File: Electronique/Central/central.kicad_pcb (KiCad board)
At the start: 2 copper layers, 173 x 90 mm, 66 parts, among them P1 CONN_02X03, P10 CONN_Selec, P11 CONN_01X02, P12 CONN_01X02, P13 CONN_01X02, P14 CONN_01X02, P15 CONN_01X02, P2 CONN_Speaker, P3 CONN_jack, P4 CONN_jacky_led, P5 CONN_LED, P6 CONN_02X03, P7 CONN_02X03, P8 CONN_02X03, P9 CONN_jack_start, Q1 IRF540N, Q2 Q_NMOS_DGS, Q3 Q_NMOS_DGS, U1 Nucleo-64, U10 trou-d3mm, U11 trou-d3mm, U12 trou-d3mm, U13 trou-d3mm, U14 trou-d3mm, U15 trou-d3mm, U2 LM317_SOT223, U3 LM317_SOT223, U4 TDA6205, U5 B_Plug_5mm, U6 B_Plug_5mm, U7 DSN2596, U8 DSN2596, U9 MC34152

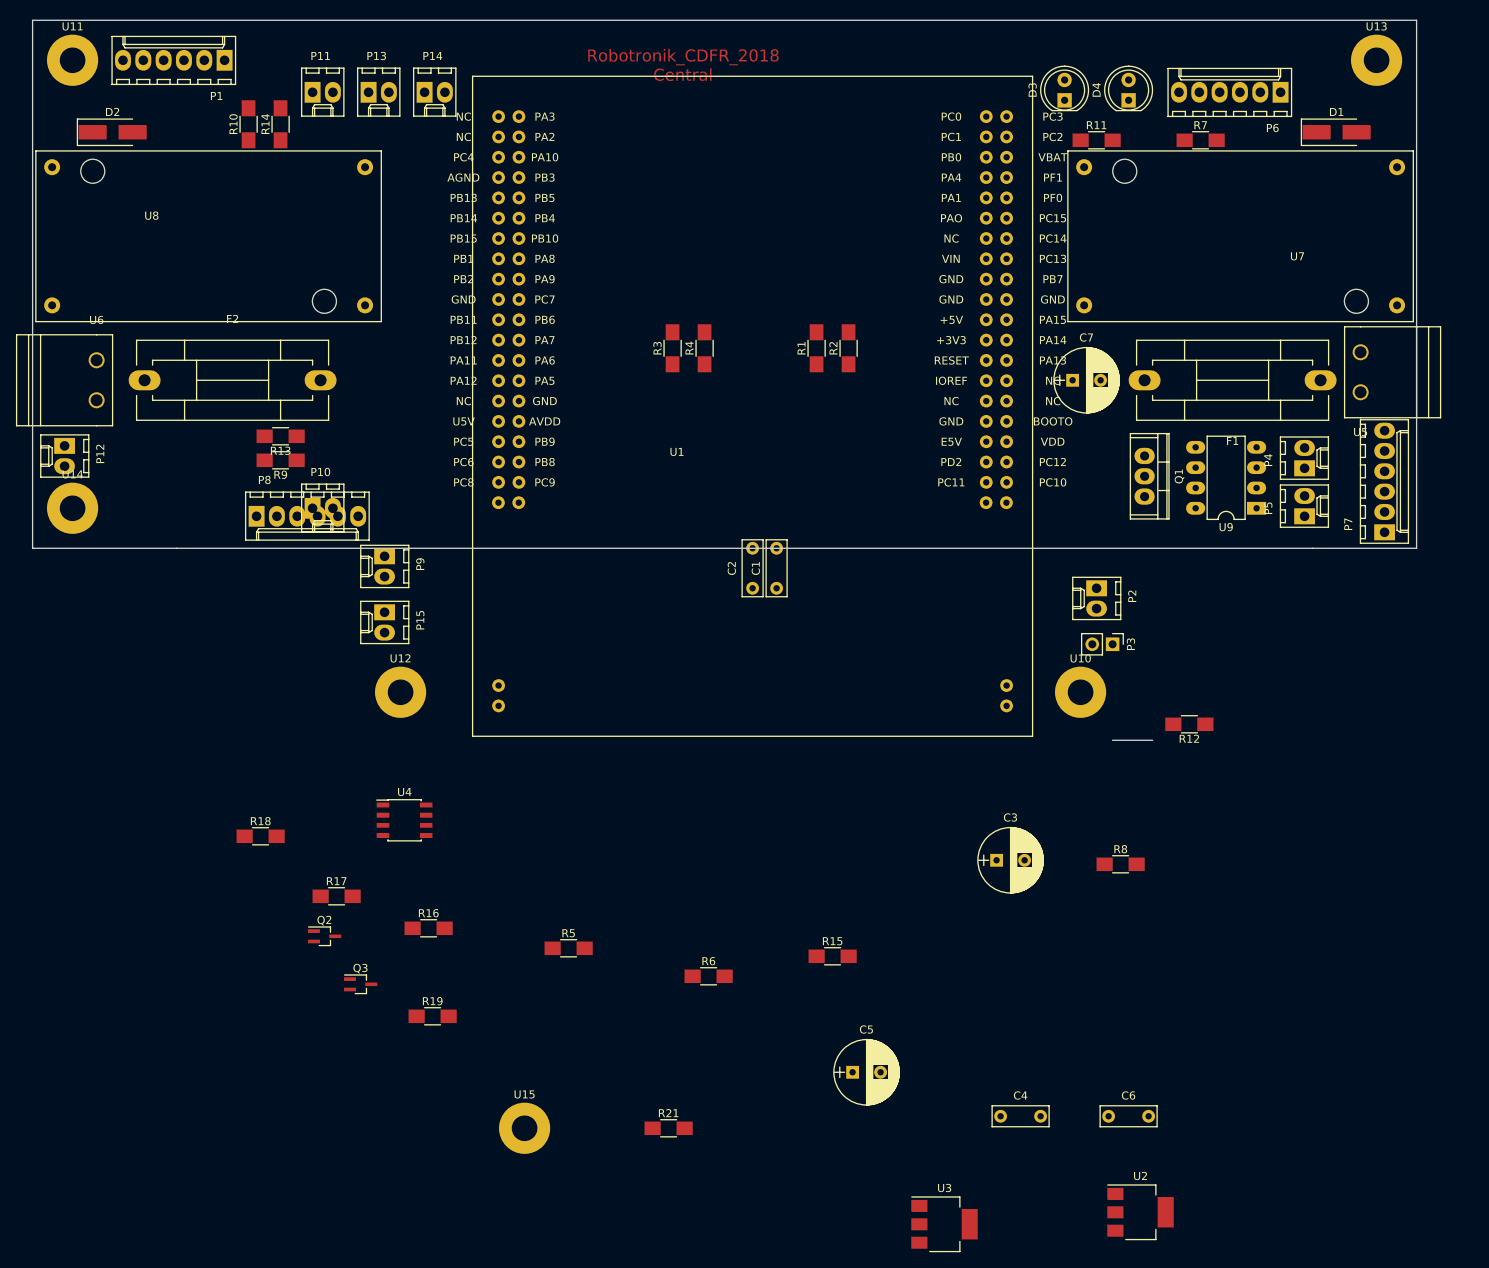
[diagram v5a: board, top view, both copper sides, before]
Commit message: Central : placement
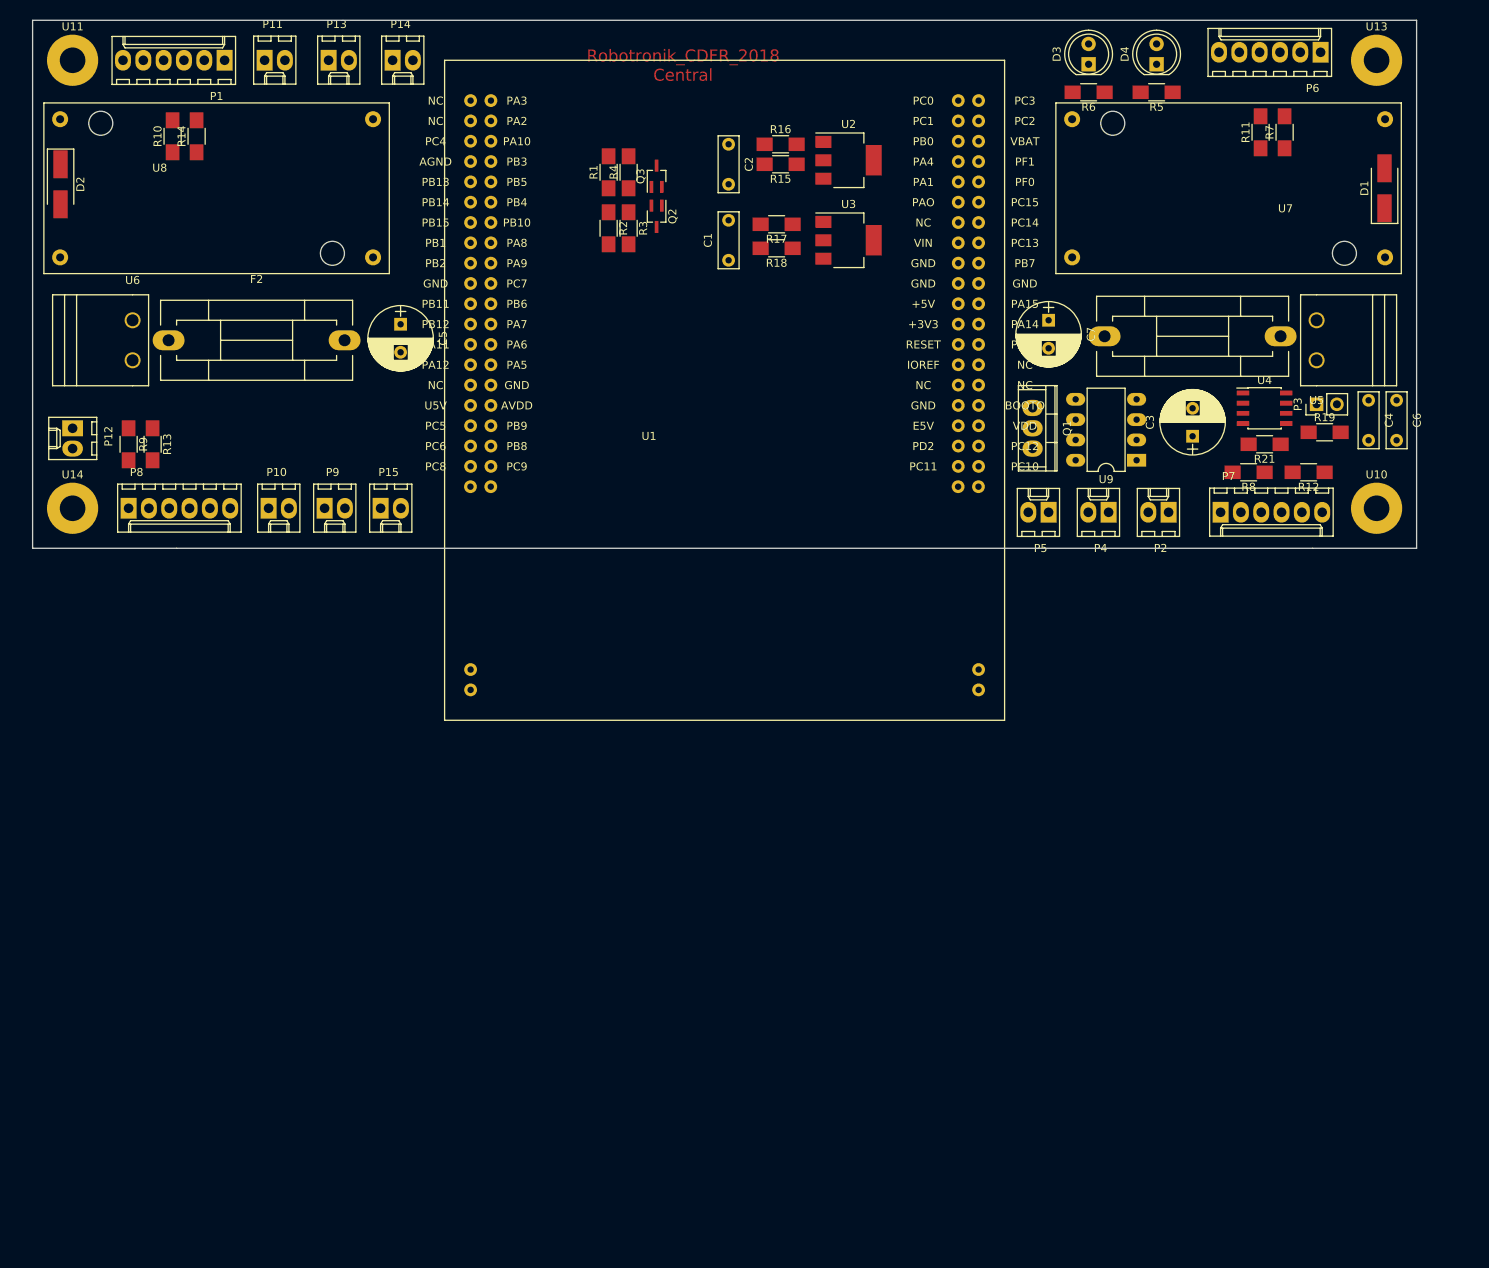
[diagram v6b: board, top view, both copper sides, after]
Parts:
- removed U12, U15: trou-d3mm, Mounting_Holes:MountingHole_3.2mm_M3_Pad
- moved U2 136.5 mm to (168.0, 85.5)
- moved R19 133.3 mm to (227.5, 119.5)
- moved R5 129.8 mm to (206.5, 77.0), turned to 180 degrees
- moved U3 123.6 mm to (168.0, 95.5)
- moved R6 120.3 mm to (198.0, 77.0), turned to 180 degrees
- moved U4 119.2 mm to (220.0, 116.5)
- moved R21 113.4 mm to (220.0, 121.0), turned to 180 degrees
- moved C5 109.2 mm to (112.0, 106.0), turned to 270 degrees
- moved Q3 107.6 mm to (144.0, 87.5), turned to 90 degrees
- moved R16 107.4 mm to (159.5, 83.5)
- moved C4 100.6 mm to (233.0, 115.5), turned to 270 degrees
- moved R17 100.4 mm to (159.0, 93.5), turned to 180 degrees
- moved R15 99.2 mm to (159.5, 86.0), turned to 180 degrees
- moved Q2 99.1 mm to (144.0, 92.5), turned to 270 degrees
- moved R18 97.8 mm to (159.0, 96.5), turned to 180 degrees
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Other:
- board size 173 x 90 mm -> 173 x 66 mm
- rule via_min_size: 0.4 -> 0.6

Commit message: Central routage
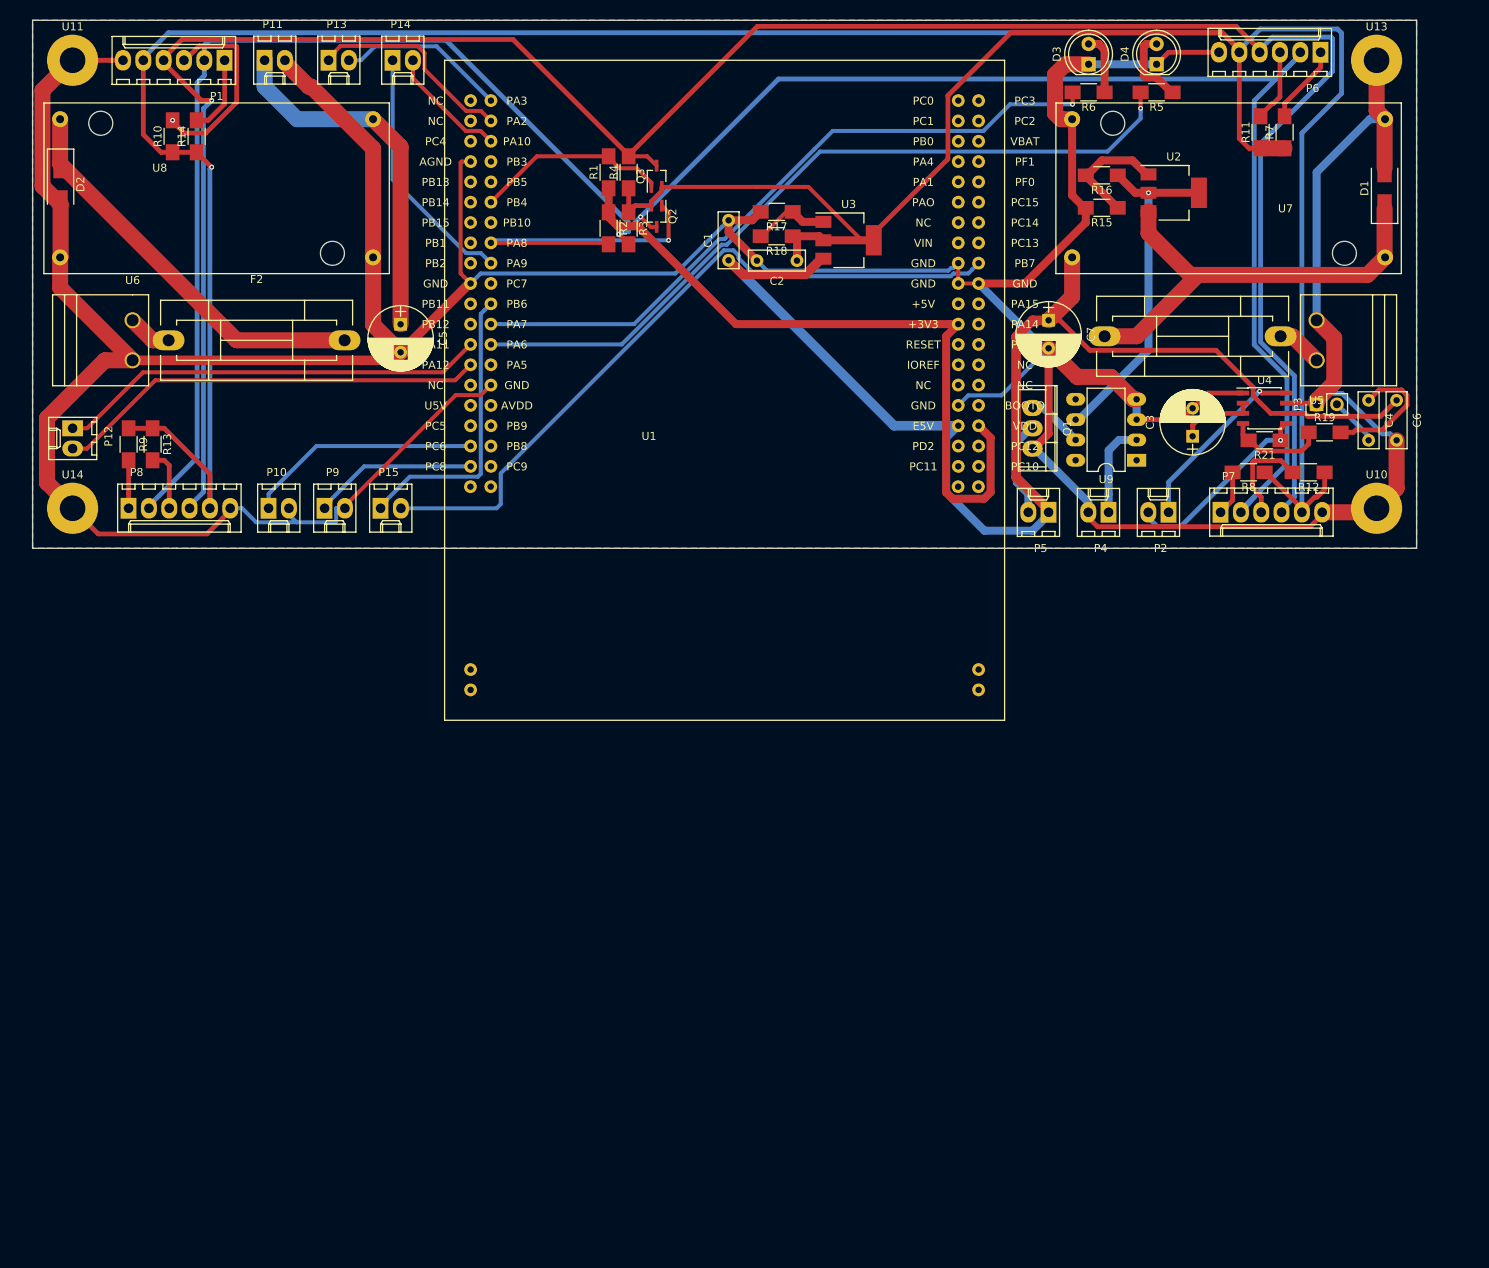
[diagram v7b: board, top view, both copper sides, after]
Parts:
- moved U2 40.8 mm to (208.6, 89.6)
- moved R15 40.5 mm to (199.6, 91.4)
- moved R16 40.3 mm to (199.6, 87.4), turned to 180 degrees
- moved C2 16.9 mm to (161.5, 98.0), turned to 180 degrees
- moved R17 1.55 mm to (159.0, 91.9)
- moved R18 1.50 mm to (159.0, 95.0)
- moved R21 0.50 mm to (220.0, 120.5)
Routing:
- net GND: track 0.00 -> 587.7 mm
- net +2.8V: track 0.00 -> 440.1 mm, vias 0 -> 1
- net Net-(P1-Pad4): track 0.00 -> 292.5 mm, vias 0 -> 1
- net Net-(P1-Pad2): track 0.00 -> 291.2 mm, vias 0 -> 2
- net +5V: track 0.00 -> 163.1 mm
- net Net-(R5-Pad2): track 0.00 -> 96.2 mm, vias 0 -> 1
- net I2C_Free_SDA: track 0.00 -> 90.0 mm
- net +3V3: track 0.00 -> 89.7 mm
- net Net-(R6-Pad2): track 0.00 -> 85.6 mm, vias 0 -> 1
- net BATT: track 0.00 -> 56.4 mm
- net /Pince_TX: track 0.00 -> 54.1 mm
- net /Pince_RX: track 0.00 -> 54.1 mm
- net Net-(D2-Pad1): track 0.00 -> 50.3 mm
- net /Power/Rasp_power: track 0.00 -> 45.6 mm
- net +9V: track 0.00 -> 43.8 mm, vias 0 -> 1
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- added copper zone on B.Cu, net GND
- added copper zone on F.Cu, net GND
